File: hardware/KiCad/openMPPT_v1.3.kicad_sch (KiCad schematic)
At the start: 0 parts

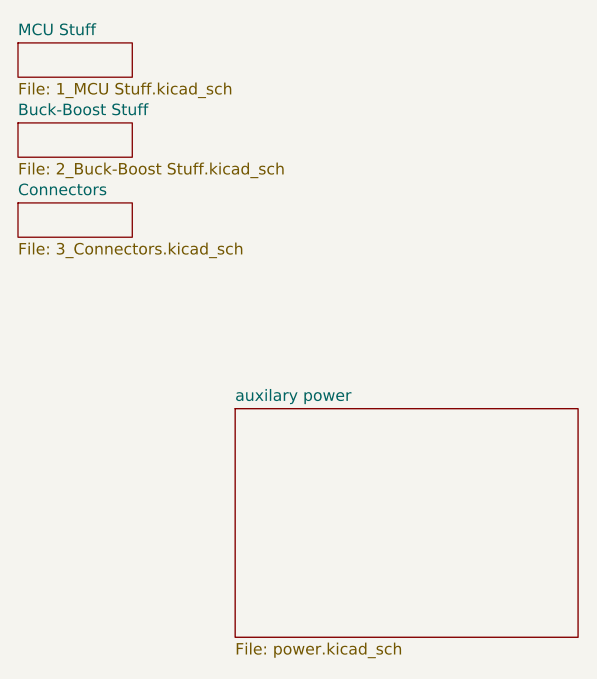
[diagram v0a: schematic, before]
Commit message: Vendor easyeda2kicad component library; rename project files; fix stale part data
Vendors the 16 easyeda2kicad:* parts (symbols/footprints/3D models) that
were referenced but never committed, registers them in sym-lib-table and
a new fp-lib-table, and adds the EASYEDA2KICAD project text variable so
existing 3D-model paths resolve.

Also corrects BSC030N08NS5's stale metadata (was pointing at an ElecSuper
clone, C49108769, instead of the genuine Infineon part, C501507) and
swaps its footprint to the freshly-fetched one, and fixes STANDARDS.md's
Hardware Universe table (stale reference designators, stale MOSFET/
CC6937 LCSC numbers, ~13 previously undocumented parts, wrong library
path).

Renames the auto-generated project/sheet filenames to something legible:
ProPrj_STM32 MPPT_2024-07-25_15-40-35_2026-05-30.* -> openMPPT_v1.3.*,
and the numbered "N_Name Stuff.kicad_sch" sheets -> mcu/buck_boost/
connectors.kicad_sch. Verified via kicad-cli ERC/DRC before and after -
same violation counts, no structural breakage.

Co-Authored-By: Claude Sonnet 5 <noreply@anthropic.com>
Claude-Session: https://claude.ai/code/session_01FKwww6crXDCSrRUFRETJEs
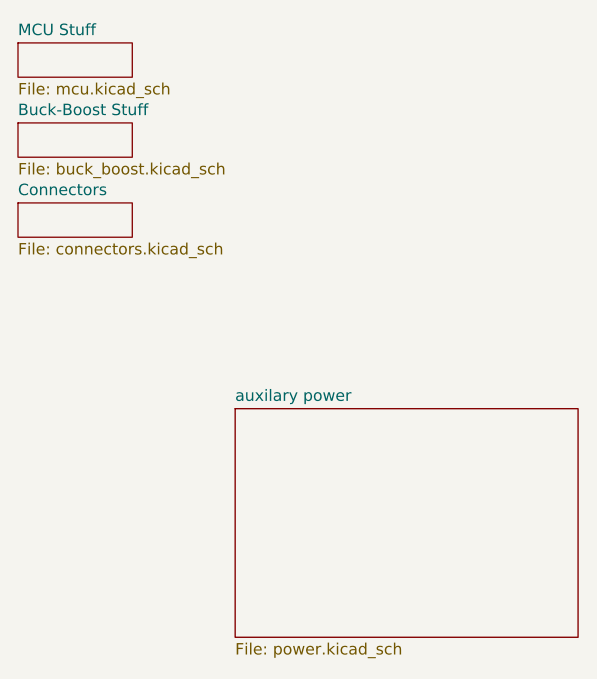
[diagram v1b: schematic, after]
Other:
- sheet Buck-Boost Stuff: file 2_Buck-Boost Stuff.kicad_sch -> buck_boost.kicad_sch
- sheet Connectors: file 3_Connectors.kicad_sch -> connectors.kicad_sch
- sheet MCU Stuff: file 1_MCU Stuff.kicad_sch -> mcu.kicad_sch
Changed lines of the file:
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@@
 			)
 		)
-		(property "Sheetfile" "2_Buck-Boost Stuff.kicad_sch"
+		(property "Sheetfile" "buck_boost.kicad_sch"
 			(at 5.08 18.3646 0)
 			(show_name no)
@@
 		)
 		(instances
-			(project "ProPrj_STM32 MPPT_2024-07-25_15-40-35_2026-05-30"
+			(project "openMPPT_v1.3"
 				(path "/b4d74b55-d9ad-45d1-9f37-bb84a2194cf7"
 					(page "2")
@@
 			)
 		)
-		(property "Sheetfile" "1_MCU Stuff.kicad_sch"
+		(property "Sheetfile" "mcu.kicad_sch"
 			(at 5.08 9.4746 0)
 			(show_name no)
@@
 		)
 		(instances
-			(project "ProPrj_STM32 MPPT_2024-07-25_15-40-35_2026-05-30"
+			(project "openMPPT_v1.3"
 				(path "/b4d74b55-d9ad-45d1-9f37-bb84a2194cf7"
 					(page "1")
@@
 			)
 		)
-		(property "Sheetfile" "3_Connectors.kicad_sch"
+		(property "Sheetfile" "connectors.kicad_sch"
 			(at 5.08 27.2546 0)
 			(show_name no)
@@
 		)
 		(instances
-			(project "ProPrj_STM32 MPPT_2024-07-25_15-40-35_2026-05-30"
+			(project "openMPPT_v1.3"
 				(path "/b4d74b55-d9ad-45d1-9f37-bb84a2194cf7"
 					(page "3")
@@
 		)
 		(instances
-			(project "ProPrj_STM32 MPPT_2024-07-25_15-40-35_2026-05-30"
+			(project "openMPPT_v1.3"
 				(path "/b4d74b55-d9ad-45d1-9f37-bb84a2194cf7"
 					(page "4")
